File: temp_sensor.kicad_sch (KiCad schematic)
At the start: 7 parts, among them U4 PCT2075DP

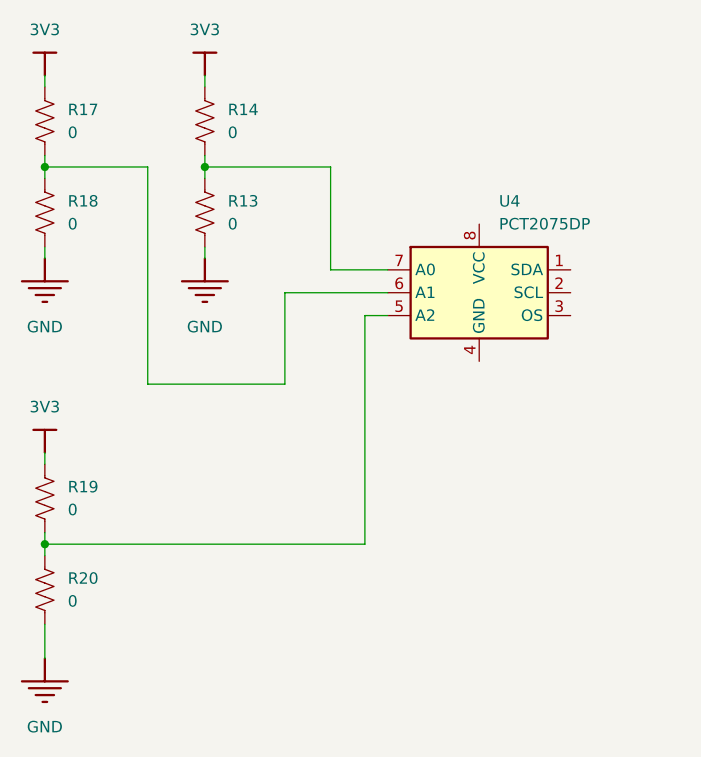
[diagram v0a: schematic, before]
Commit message: updated top level schematic for MEB
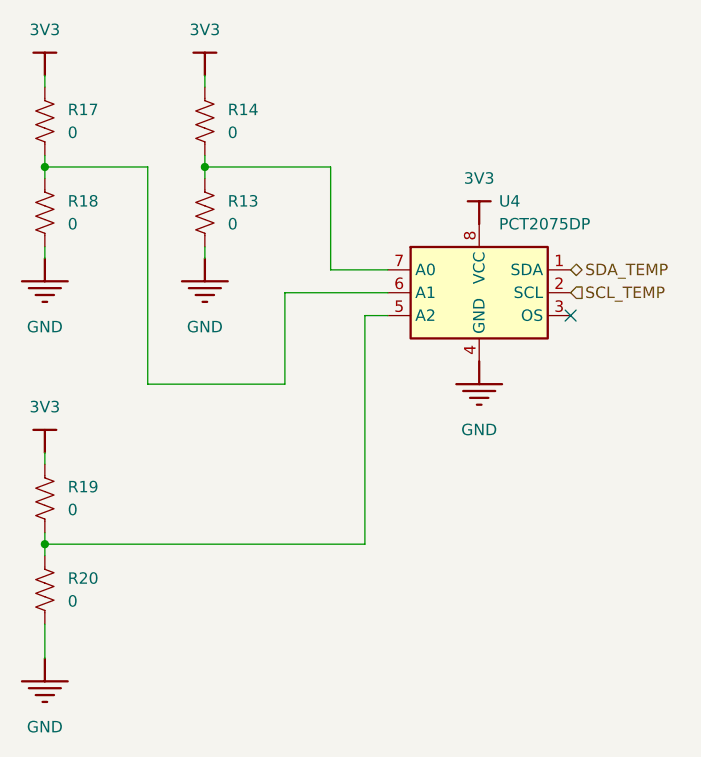
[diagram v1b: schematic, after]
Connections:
- net 3V3: now also U4.8 (VCC)
- net GND: now also U4.4 (GND)
- net SDA_TEMP: now reaches U4.1 (SDA)
- net SCL_TEMP: now reaches U4.2 (SCL)
- no-connect marks 0 -> 1
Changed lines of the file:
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@@
   (junction (at 102.87 87.63) (diameter 0) (color 0 0 0 0)
   )
+  (no_connect (at 161.29 104.14))
   (wire (pts (xy 102.87 128.27) (xy 102.87 129.54))
     (stroke (width 0) (type default))
@@
   (wire (pts (xy 134.62 87.63) (xy 134.62 99.06))
     (stroke (width 0) (type default))
+  )
+  (hierarchical_label "SDA_TEMP" (shape bidirectional) (at 161.29 99.06 0) (fields_autoplaced)
+    (effects (font (size 1.27 1.27)) (justify left))
+  )
+  (hierarchical_label "SCL_TEMP" (shape input) (at 161.29 101.6 0) (fields_autoplaced)
+    (effects (font (size 1.27 1.27)) (justify left))
   )
   (symbol (lib_id "Sensor_Temperature:PCT2075DP") (at 151.13 101.6 0) (unit 1)
@@
     )
   )
+  (symbol (lib_id "MEB-altium-import:GND") (at 151.13 109.22 0) (unit 1)
+    (in_bom yes) (on_board yes) (dnp no)
+    (property "Reference" "#PWR027" (at 151.13 104.14 0)
+      (effects (font (size 1.27 1.27)) hide)
+    )
+    (property "Value" "GND" (at 151.13 116.84 0)
+      (effects (font (size 1.27 1.27)))
+    )
+    (property "Footprint" "" (at 151.13 109.22 0)
+      (effects (font (size 1.27 1.27)) hide)
+    )
+    (property "Datasheet" "" (at 151.13 109.22 0)
+      (effects (font (size 1.27 1.27)) hide)
+    )
+    (pin "")
+    (instances
+      (project "MEB"
+        (path "/228e4997-23c1-4c21-939b-583cad26a5e3/fa265f0a-160e-4a62-aa89-b135824d6d77"
+          (reference "#PWR027") (unit 1)
+        )
+      )
+    )
+  )
   (symbol (lib_id "Device:R_US") (at 102.87 82.55 0) (unit 1)
     (in_bom yes) (on_board yes) (dnp no) (fields_autoplaced)
@@
         )
       )
+    )
+  )
+  (symbol (lib_id "MEB-altium-import:3V3") (at 151.13 93.98 180) (unit 1)
+    (in_bom yes) (on_board yes) (dnp no)
+    (property "Reference" "#PWR026" (at 151.13 96.52 0)
+      (effects (font (size 1.27 1.27)) hide)
+    )
+    (property "Value" "3V3" (at 151.13 88.9 0)
+      (effects (font (size 1.27 1.27)))
+    )
+    (property "Footprint" "" (at 151.13 93.98 0)
+      (effects (font (size 1.27 1.27)) hide)
+    )
+    (property "Datasheet" "" (at 151.13 93.98 0)
+      (effects (font (size 1.27 1.27)) hide)
+    )
+    (pin "")
+    (instances
+      (project "MEB"
+        (path "/228e4997-23c1-4c21-939b-583cad26a5e3/fa265f0a-160e-4a62-aa89-b135824d6d77"
+          (reference "#PWR026") (unit 1)
+        )
+      )

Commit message: updated power and ground symbols in schematic to kicad library version
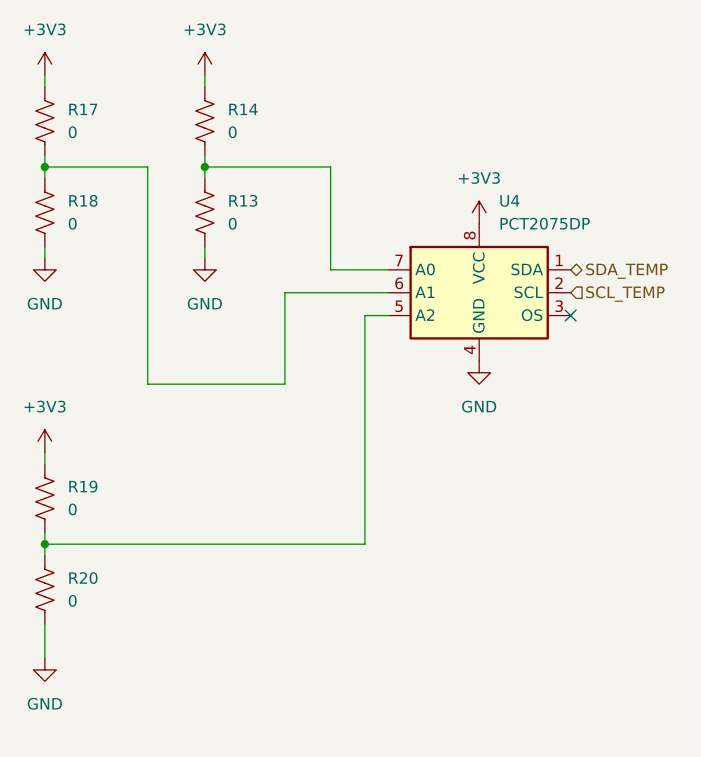
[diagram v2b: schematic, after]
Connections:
- net 3V3 renamed +3V3
